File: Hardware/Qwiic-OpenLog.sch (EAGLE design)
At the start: 30 parts, among them J1 MICRO-SD, J10 GATOR, J5 ISP, J7 GATOR, J8 GATOR, J9 GATOR, Q1 16MHZ, U2 ATMEGA328P

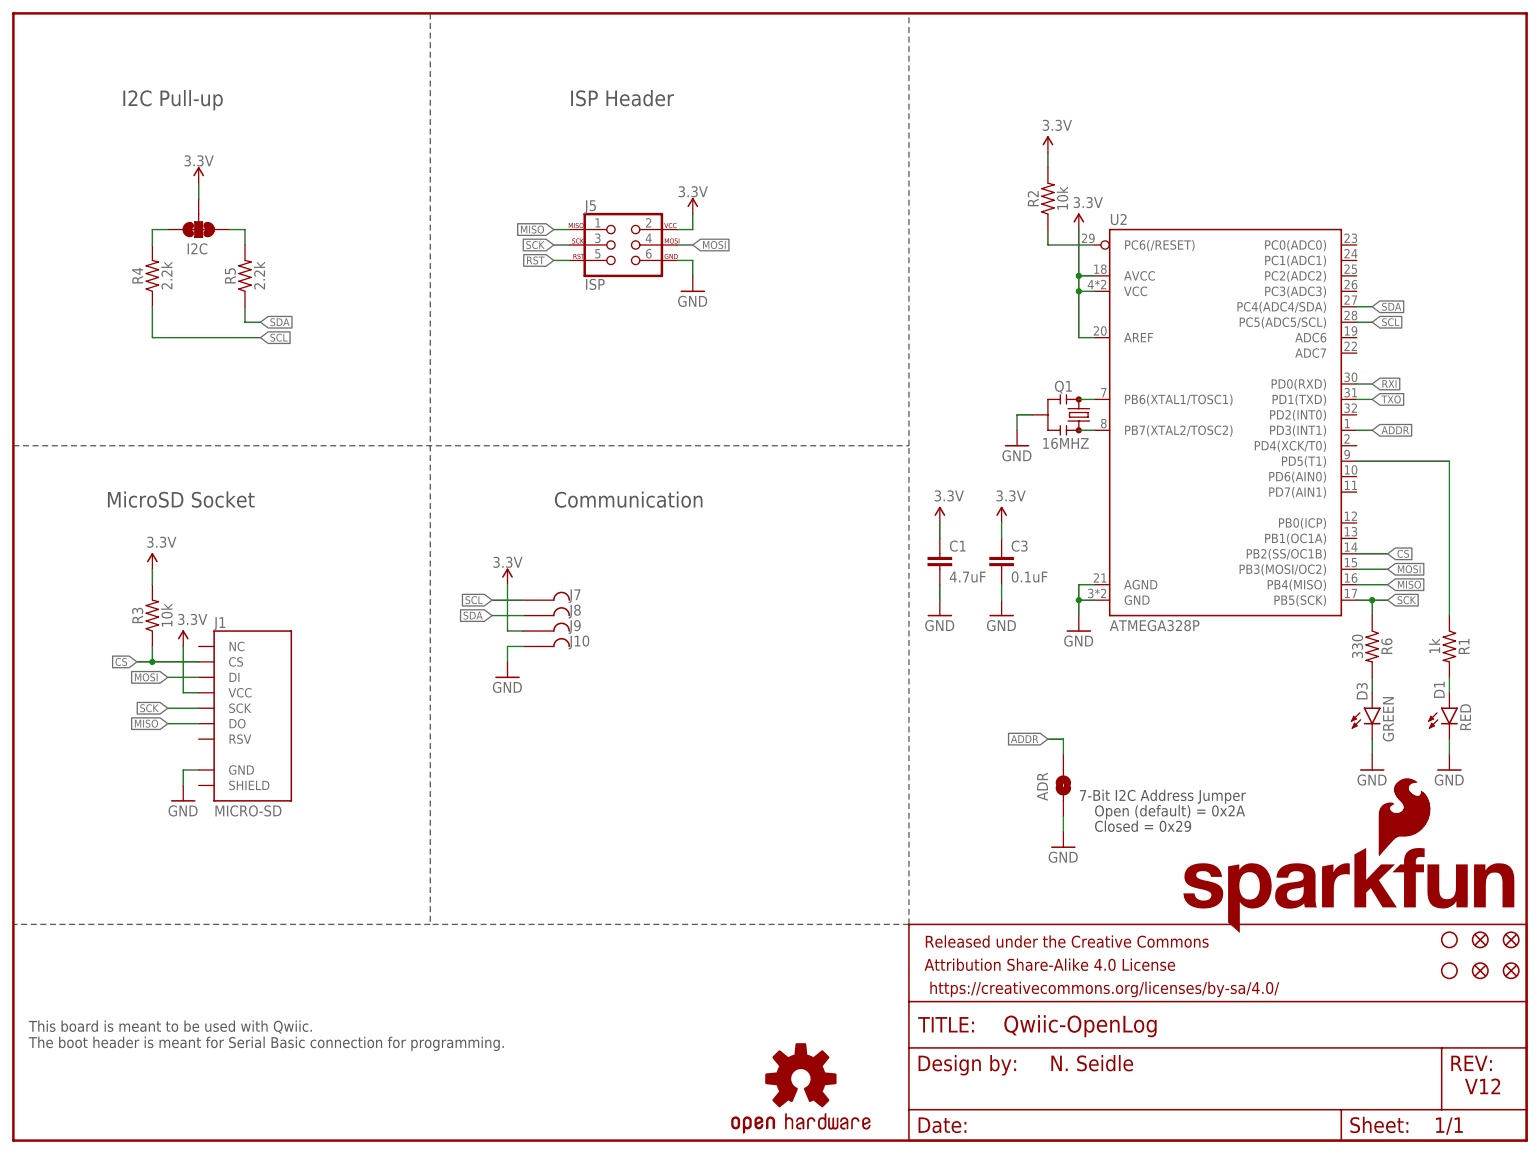
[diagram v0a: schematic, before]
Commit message: initial layout completed, needs silk
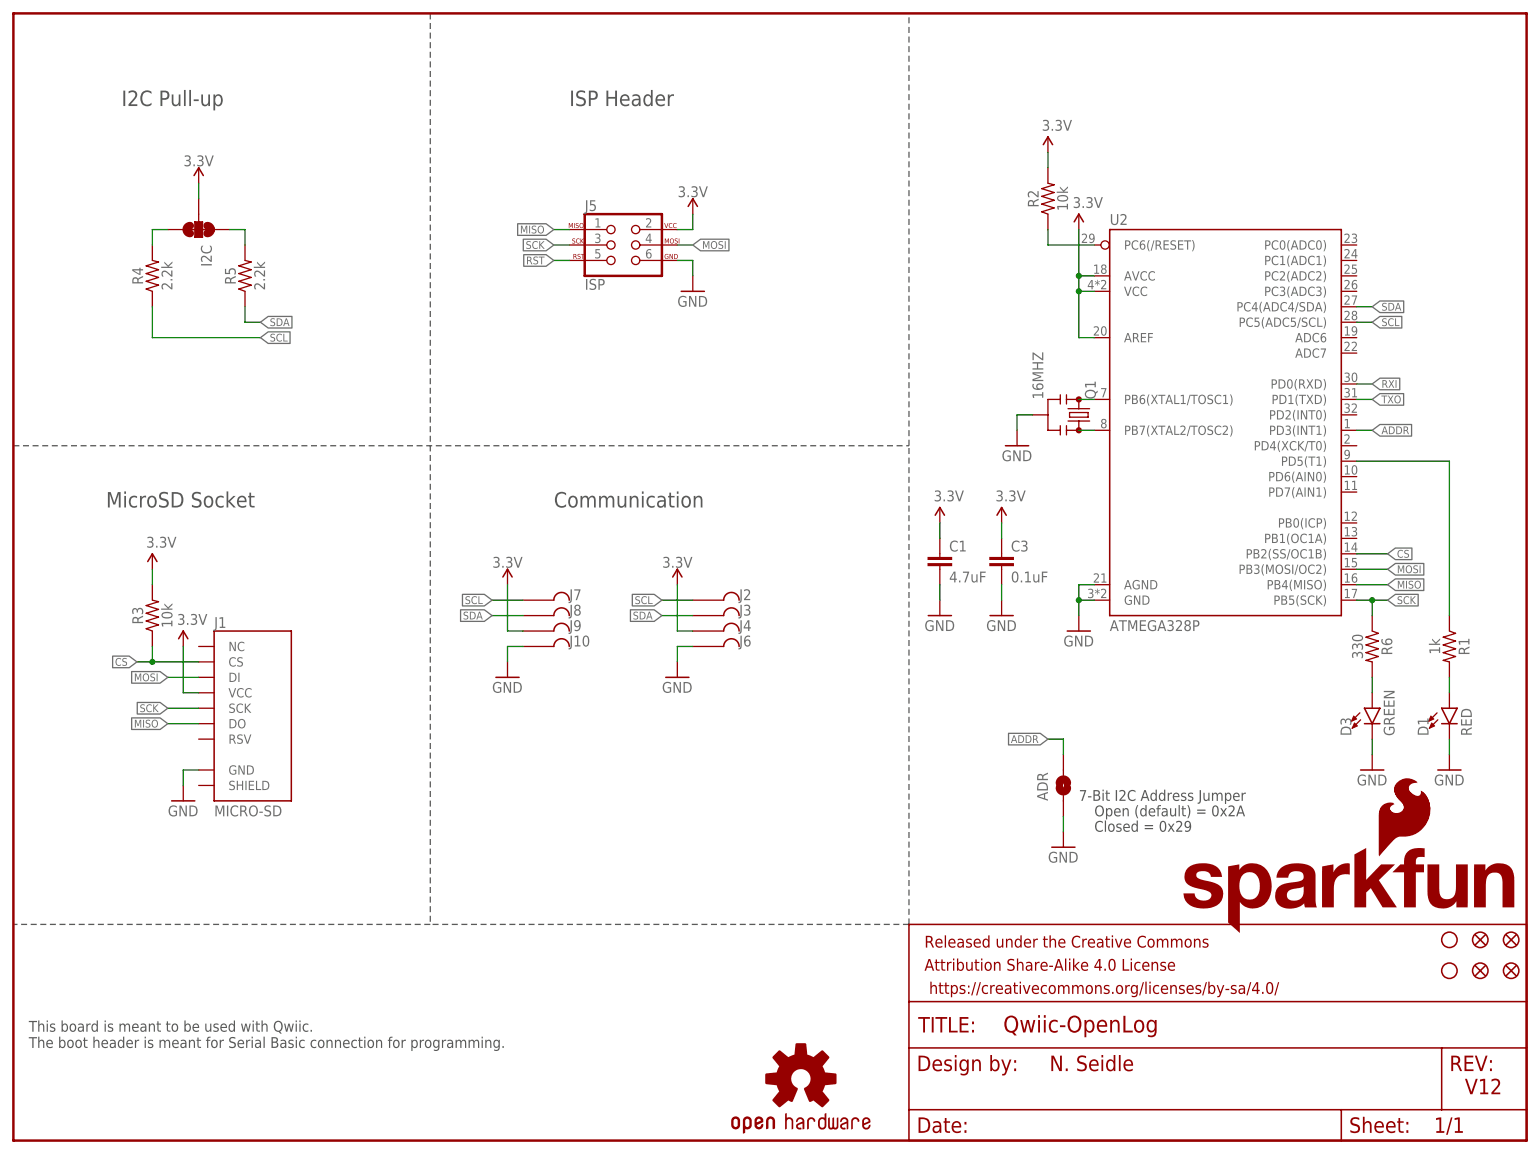
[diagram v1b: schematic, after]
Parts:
- added J2, J3, J4, J6: GATORGATOR_MINI, SparkFun-Connectors:GATORGATOR_MINI
- J10, J7, J8, J9: value GATOR -> GATORGATOR_MINI; device SparkFun-Connectors:GATOR -> SparkFun-Connectors:GATORGATOR_MINI
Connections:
- net 3.3V: now also J4.P$1
- net GND: now also J6.P$1
- net SCL: now also J2.P$1
- net SDA: now also J3.P$1

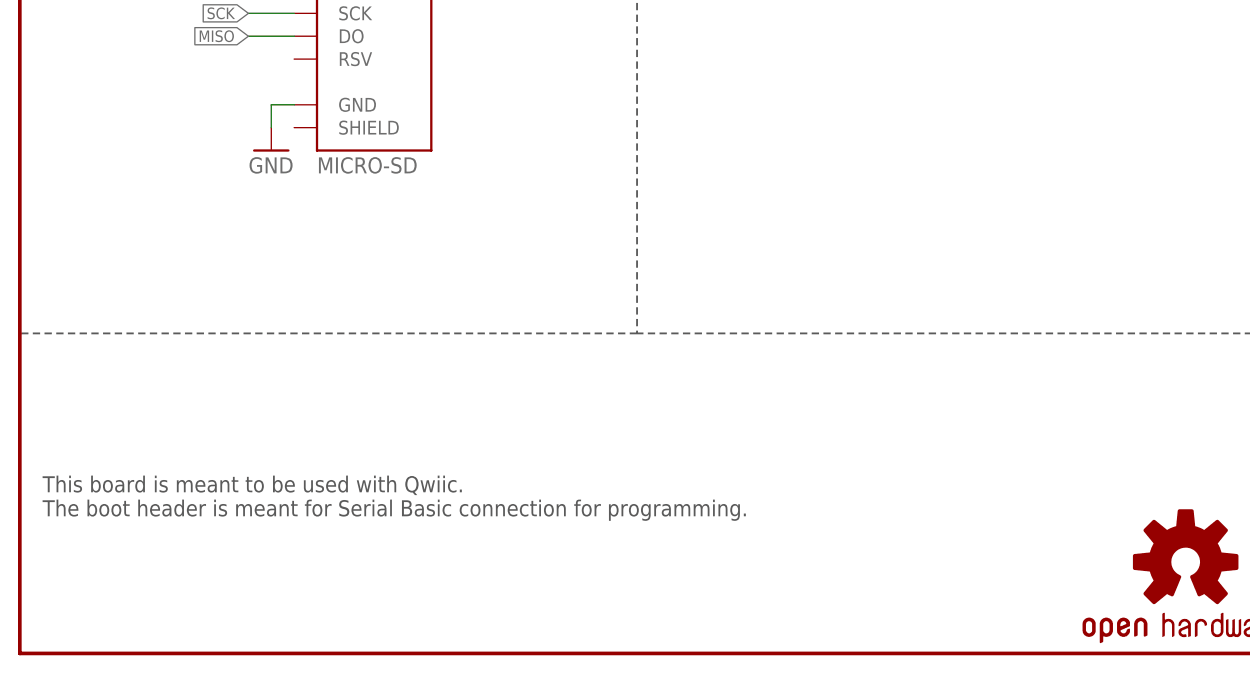
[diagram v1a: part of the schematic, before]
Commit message: adding RTC
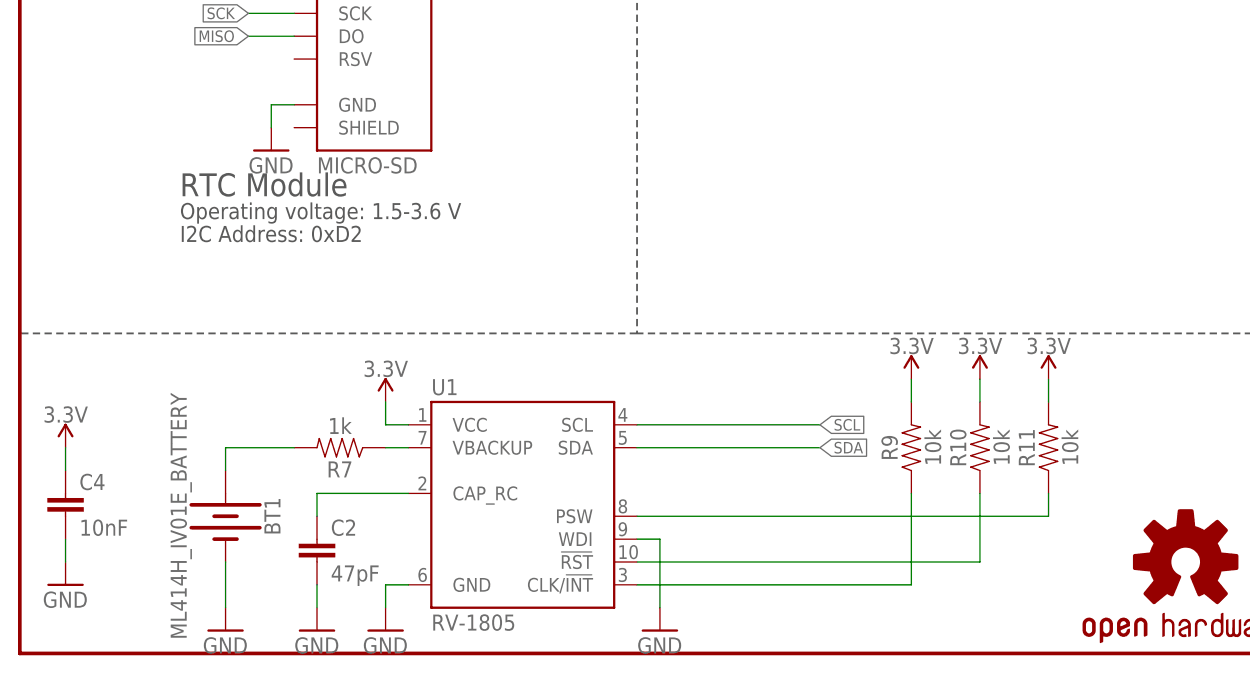
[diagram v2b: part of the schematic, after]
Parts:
- added BT1: ML414H_IV01E_BATTERY, SparkFun-Batteries:ML414H_IV01E_BATTERY
- added C2: 47pF, SparkFun-Capacitors:47PF-0603-50V-5%
- added C4: 10nF, SparkFun-Capacitors:10NF-0603-50V-10%
- added R10, R11, R9: 10k, SparkFun-Resistors:10KOHM-0603-1/10W-1%
- added R7: 1k, SparkFun-Resistors:1KOHM-0603-1/10W-1%
- added U1: RV-1805, SparkFun-Clocks:RV-1805
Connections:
- new net !INT: R9.1, U1.CLK/!INT
- new net !RST: R10.1, U1.!RST
- new net N$10: C2.1, U1.CAP_RC
- new net N$8: BT1.+, R7.2
- new net PSW: R11.1, U1.PSW
- new net VBACKUP: R7.1, U1.VBACKUP
- net 3.3V: now also C4.1, R10.2, R11.2, R9.2, U1.VCC
- net GND: now also BT1.-, C2.2, C4.2, U1.GND, U1.WDI
- net SCL: now also U1.SCL
- net SDA: now also U1.SDA
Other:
- note added: "I2C Address: 0xD2"
- note added: "Operating voltage: 1.5-3.6 V"
- note added: "RTC Module"
- note removed: "This board is meant to be used with Qwiic. The boot header is meant for Serial Basic connection for programming."

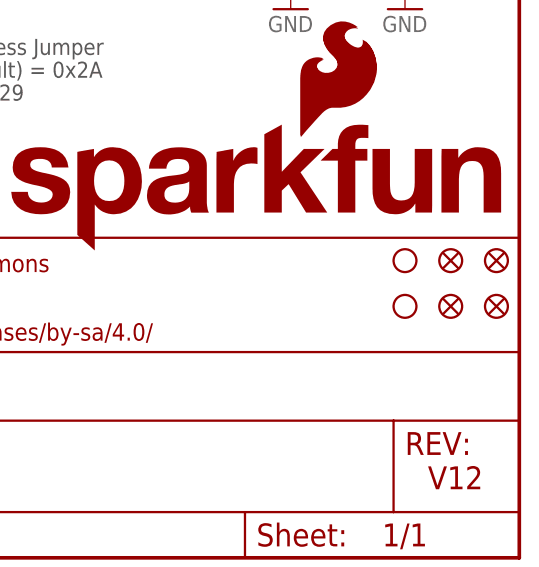
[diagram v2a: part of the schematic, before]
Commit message: updating silk, adding rtc
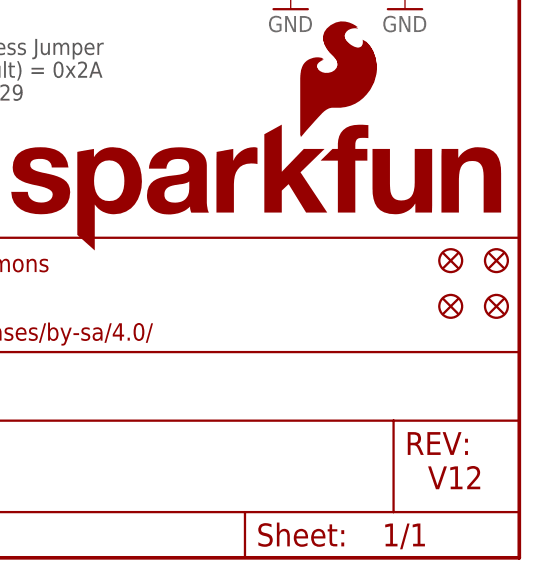
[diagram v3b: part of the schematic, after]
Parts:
- removed JP3, JP4: STAND-OFF, SparkFun:STAND-OFF
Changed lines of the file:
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@@
 <part name="I2C" library="SparkFun-Jumpers" deviceset="JUMPER-SMT_3_2-NC_TRACE" device="_SILK" value=""/>
 <part name="SUPPLY1" library="SparkFun-PowerSymbols" deviceset="3.3V" device=""/>
-<part name="JP3" library="SparkFun" deviceset="STAND-OFF" device=""/>
-<part name="JP4" library="SparkFun" deviceset="STAND-OFF" device=""/>
 <part name="J5" library="SparkFun-Connectors" deviceset="AVR_SPI_PROG_3X2" device="TESTPOINTS" value="ISP"/>
 <part name="SUPPLY2" library="SparkFun-PowerSymbols" deviceset="3.3V" device=""/>
@@
 <attribute name="VALUE" x="30.48" y="160.274" size="1.778" layer="96" align="bottom-center"/>
 </instance>
-<instance part="JP3" gate="G$1" x="236.22" y="33.02" smashed="yes"/>
-<instance part="JP4" gate="G$1" x="236.22" y="27.94" smashed="yes"/>
 <instance part="J5" gate="G$1" x="99.06" y="147.32" smashed="yes">
 <attribute name="NAME" x="93.98" y="152.908" size="1.778" layer="95" font="vector"/>
